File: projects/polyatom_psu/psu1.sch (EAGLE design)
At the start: 2 parts

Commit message: completed psu
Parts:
- added BR1, BR2: (no value), STM_Library:GBU4J
- added C10, C11, C12, C13, C14, C15, C5, C8, C9: 100n, eagle-ltspice:CC1206
- added C100, C2: 1000u, rcl:CPOL-EUE5-13
- added C16, C17, C20, C21: 10u, capacitor-wima:C7.5/3
- added C18: 100n, rcl:C-USC1206
- added C19: 1u, rcl:C-USC1206
- added C3: 0.22u, rcl:C-USC1206
- added C4: 2.2u, rcl:C-USC1206
- added D1, D2: HLMP6, display-hp:HLMP6
- added D3, D4: 1N4004, diode:1N4004
- added R1, R3: 680, eagle-ltspice:R0207/10
- added U$3, U$4, U$5: BANANA, STM_Library:BANANA
- added U$8: TERMINALBLOCK, STM_Library:TERMINALBLOCK
- U$1: value GBU4J -> LM7815; device STM_Library:GBU4J -> STM_Library:LM7815
- U$2: value GBU4J -> LM7915; device STM_Library:GBU4J -> STM_Library:LM7915
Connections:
- new net +15V: C10.1, C11.1, C16.1, C17.1, C18.1, C5.1, C8.1, C9.1, D3.C, R1.2, U$1.P$1, U$3.P$1
- new net -15V: C12.2, C13.2, C14.2, C15.2, C19.2, C20.2, C21.2, D1.K, D4.A, U$2.P$1, U$5.P$1
- new net GND: BR1.P$4, BR2.P$1, C10.2, C100.-, C11.2, C12.1, C13.1, C14.1, C15.1, C16.2, C17.2, C18.2, C19.1, C2.+, C20.1, C21.1, C3.2, C4.1, C5.2, C8.2, C9.2, D2.K, D3.A, D4.C, R3.2, U$1.P$2, U$2.P$2, U$4.P$1, U$8.P$3
- new net N$10: BR2.P$2, U$8.P$2
- new net N$11: BR2.P$3, U$8.P$1
- new net N$2: D2.A, R1.1
- new net N$4: D1.A, R3.1
- new net N$8: BR1.P$2, U$8.P$5
- new net N$9: BR1.P$3, U$8.P$4
- new net NEG: BR2.P$4, C2.-, C4.2, U$2.P$3
- new net POS: BR1.P$1, C100.+, C3.1, U$1.P$3

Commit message: added top and bottom pour, caps renamed
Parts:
- removed C20, C21: 10u, capacitor-wima:C7.5/3
- added C6, C7: 100n, eagle-ltspice:CC1206
- added GND, V2: (no value), wirepad:3,81/1,1
- C11: value 100n -> 1000u; device eagle-ltspice:CC1206 -> rcl:CPOL-EUE5-13
- C12: value 100n -> 2.2u; device eagle-ltspice:CC1206 -> rcl:C-USC1206
- C13: value 100n -> 1u; device eagle-ltspice:CC1206 -> rcl:C-USC1206
- C14, C15, C5: value 100n -> (none); device eagle-ltspice:CC1206 -> rcl:CPOL-USTT2D5
- C16, C17: value 10u -> 100n; device capacitor-wima:C7.5/3 -> eagle-ltspice:CC1206
- C18: device rcl:C-USC1206 -> eagle-ltspice:CC1206
- C19: value 1u -> 100n; device rcl:C-USC1206 -> eagle-ltspice:CC1206
- C2: value 1000u -> 0.22u; device rcl:CPOL-EUE5-13 -> rcl:C-USC1206
- C3: value 0.22u -> 100n
- C4: value 2.2u -> (none); device rcl:C-USC1206 -> rcl:CPOL-USTT2D5
- renumbered C100 to C1, U$2 to U$6
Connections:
- net +15V: now also C3.1, C4.+, C5.+, C6.1, C7.1; no longer C11.1, C16.1, C17.1, C18.1, C5.1
- net -15V: now also C14.-, C15.-, C16.2, C17.2, C18.2, U$6.P$3; no longer C12.2, C14.2, C15.2, C20.2, C21.2, U$6.P$1
- net GND: now also C11.+, C14.+, C15.+, C16.1, C17.1, C18.1, C2.2, C4.-, C5.-, C6.2, C7.2, GND.P, U$6.P$1; no longer C11.2, C14.1, C15.1, C16.2, C17.2, C18.2, C2.+, C20.1, C21.1, C4.1, C5.2, U$6.P$2
- net NEG: now also C11.-, C12.2, U$6.P$2; no longer C2.-, C4.2, U$6.P$3
- net POS: now also C2.1, V2.P; no longer C3.1
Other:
- moved on the sheet: C10, C12, C13, C16, C17, C18, C19, C3, C8, C9

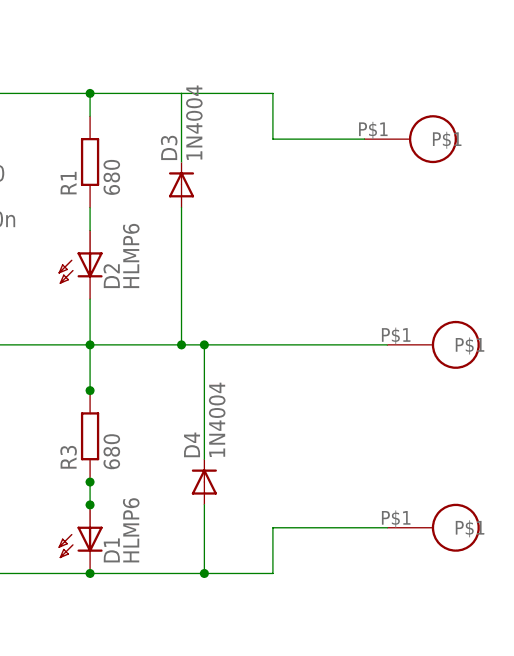
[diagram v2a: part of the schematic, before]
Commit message: added text to the top and bottom of board
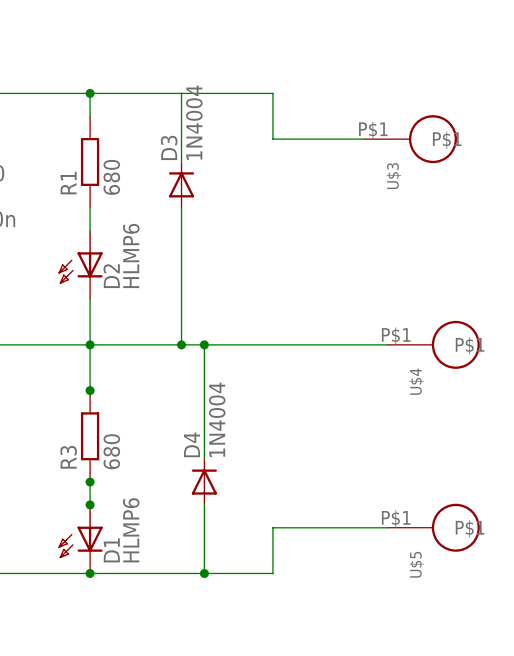
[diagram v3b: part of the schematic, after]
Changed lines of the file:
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@@
 <?xml version="1.0" encoding="utf-8"?>
 <!DOCTYPE eagle SYSTEM "eagle.dtd">
-<eagle version="9.2.2">
+<eagle version="9.2.0">
 <drawing>
 <settings>
@@
 </plain>
 <instances>
-<instance part="C1" gate="G$1" x="55.88" y="66.04" smashed="yes">
+<instance part="C1" gate="G$1" x="55.88" y="66.04">
 <attribute name="NAME" x="57.023" y="66.5226" size="1.778" layer="95"/>
 <attribute name="VALUE" x="57.023" y="61.4426" size="1.778" layer="96"/>
 </instance>
-<instance part="C11" gate="G$1" x="55.88" y="33.02" smashed="yes">
+<instance part="C11" gate="G$1" x="55.88" y="33.02">
 <attribute name="NAME" x="57.023" y="33.5026" size="1.778" layer="95"/>
 <attribute name="VALUE" x="57.023" y="28.4226" size="1.778" layer="96"/>
 </instance>
-<instance part="D1" gate="A" x="170.18" y="25.4" smashed="yes">
+<instance part="D1" gate="A" x="170.18" y="25.4">
 <attribute name="NAME" x="173.482" y="23.876" size="1.778" layer="95" rot="R90"/>
 <attribute name="VALUE" x="175.641" y="23.876" size="1.778" layer="96" rot="R90"/>
 </instance>
-<instance part="D2" gate="A" x="170.18" y="55.88" smashed="yes">
+<instance part="D2" gate="A" x="170.18" y="55.88">
 <attribute name="NAME" x="173.482" y="54.356" size="1.778" layer="95" rot="R90"/>
 <attribute name="VALUE" x="175.641" y="54.356" size="1.778" layer="96" rot="R90"/>
 </instance>
-<instance part="D3" gate="1" x="180.34" y="66.04" smashed="yes" rot="R90">
+<instance part="D3" gate="1" x="180.34" y="66.04" rot="R90">
 <attribute name="NAME" x="179.8574" y="68.58" size="1.778" layer="95" rot="R90"/>
 <attribute name="VALUE" x="182.6514" y="68.58" size="1.778" layer="96" rot="R90"/>
 </instance>
-<instance part="D4" gate="1" x="182.88" y="33.02" smashed="yes" rot="R90">
+<instance part="D4" gate="1" x="182.88" y="33.02" rot="R90">
 <attribute name="NAME" x="182.3974" y="35.56" size="1.778" layer="95" rot="R90"/>
 <attribute name="VALUE" x="185.1914" y="35.56" size="1.778" layer="96" rot="R90"/>
 </instance>
-<instance part="U$3" gate="J$1" x="208.28" y="71.12" smashed="yes" rot="R270"/>
-<instance part="U$4" gate="J$1" x="210.82" y="48.26" smashed="yes" rot="R270"/>
-<instance part="U$5" gate="J$1" x="210.82" y="27.94" smashed="yes" rot="R270"/>
-<instance part="C2" gate="G$1" x="66.04" y="63.5" smashed="yes">
+<instance part="U$3" gate="J$1" x="208.28" y="71.12" rot="R270"/>
+<instance part="U$4" gate="J$1" x="210.82" y="48.26" rot="R270"/>
+<instance part="U$5" gate="J$1" x="210.82" y="27.94" rot="R270"/>
+<instance part="C2" gate="G$1" x="66.04" y="63.5">
 <attribute name="NAME" x="67.056" y="64.135" size="1.778" layer="95"/>
 <attribute name="VALUE" x="67.056" y="59.309" size="1.778" layer="96"/>
 </instance>
-<instance part="C12" gate="G$1" x="66.04" y="33.02" smashed="yes">
+<instance part="C12" gate="G$1" x="66.04" y="33.02">
 <attribute name="NAME" x="67.056" y="33.655" size="1.778" layer="95"/>
 <attribute name="VALUE" x="67.056" y="28.829" size="1.778" layer="96"/>
 </instance>
-<instance part="C3" gate="G$1" x="93.98" y="66.04" smashed="yes">
+<instance part="C3" gate="G$1" x="93.98" y="66.04">
 <attribute name="NAME" x="94.996" y="66.675" size="1.778" layer="95"/>
 <attribute name="VALUE" x="94.996" y="61.849" size="1.778" layer="96"/>
 </instance>
-<instance part="C13" gate="G$1" x="96.52" y="33.02" smashed="yes">
+<instance part="C13" gate="G$1" x="96.52" y="33.02">
 <attribute name="NAME" x="97.536" y="33.655" size="1.778" layer="95"/>
 <attribute name="VALUE" x="97.536" y="28.829" size="1.778" layer="96"/>
 </instance>
-<instance part="C6" gate="G$1" x="124.46" y="66.04" smashed="yes">
+<instance part="C6" gate="G$1" x="124.46" y="66.04">
 <attribute name="NAME" x="125.984" y="66.421" size="1.778" layer="95"/>
 <attribute name="VALUE" x="125.984" y="61.341" size="1.778" layer="96"/>
 </instance>
-<instance part="C7" gate="G$1" x="132.08" y="66.04" smashed="yes">
+<instance part="C7" gate="G$1" x="132.08" y="66.04">
 <attribute name="NAME" x="133.604" y="66.421" size="1.778" layer="95"/>
 <attribute name="VALUE" x="133.604" y="61.341" size="1.778" layer="96"/>
 </instance>
-<instance part="C8" gate="G$1" x="139.7" y="66.04" smashed="yes">
+<instance part="C8" gate="G$1" x="139.7" y="66.04">
 <attribute name="NAME" x="141.224" y="66.421" size="1.778" layer="95"/>
 <attribute name="VALUE" x="141.224" y="61.341" size="1.778" layer="96"/>
 </instance>
-<instance part="C9" gate="G$1" x="147.32" y="66.04" smashed="yes">
+<instance part="C9" gate="G$1" x="147.32" y="66.04">
 <attribute name="NAME" x="148.844" y="66.421" size="1.778" layer="95"/>
 <attribute name="VALUE" x="148.844" y="61.341" size="1.778" layer="96"/>
 </instance>
-<instance part="C10" gate="G$1" x="154.94" y="66.04" smashed="yes">
+<instance part="C10" gate="G$1" x="154.94" y="66.04">
 <attribute name="NAME" x="156.464" y="66.421" size="1.778" layer="95"/>
 <attribute name="VALUE" x="156.464" y="61.341" size="1.778" layer="96"/>
 </instance>
-<instance part="C19" gate="G$1" x="147.32" y="33.02" smashed="yes">
+<instance part="C19" gate="G$1" x="147.32" y="33.02">
 <attribute name="NAME" x="148.844" y="33.401" size="1.778" layer="95"/>
 <attribute name="VALUE" x="148.844" y="28.321" size="1.778" layer="96"/>
 </instance>
-<instance part="C18" gate="G$1" x="139.7" y="33.02" smashed="yes">
+<instance part="C18" gate="G$1" x="139.7" y="33.02">
 <attribute name="NAME" x="141.224" y="33.401" size="1.778" layer="95"/>
 <attribute name="VALUE" x="141.224" y="28.321" size="1.778" layer="96"/>
 </instance>
-<instance part="C17" gate="G$1" x="132.08" y="33.02" smashed="yes">
+<instance part="C17" gate="G$1" x="132.08" y="33.02">
 <attribute name="NAME" x="133.604" y="33.401" size="1.778" layer="95"/>
 <attribute name="VALUE" x="133.604" y="28.321" size="1.778" layer="96"/>
 </instance>
-<instance part="C16" gate="G$1" x="124.46" y="33.02" smashed="yes">
+<instance part="C16" gate="G$1" x="124.46" y="33.02">
 <attribute name="NAME" x="125.984" y="33.401" size="1.778" layer="95"/>
 <attribute name="VALUE" x="125.984" y="28.321" size="1.778" layer="96"/>
 </instance>
-<instance part="U$8" gate="G$1" x="-22.86" y="48.26" smashed="yes" rot="R90"/>
-<instance part="R1" gate="G$1" x="170.18" y="68.58" smashed="yes" rot="R90">
+<instance part="U$8" gate="G$1" x="-22.86" y="48.26" rot="R90"/>
+<instance part="R1" gate="G$1" x="170.18" y="68.58" rot="R90">
 <attribute name="NAME" x="168.6814" y="64.77" size="1.778" layer="95" rot="R90"/>
 <attribute name="VALUE" x="173.482" y="64.77" size="1.778" layer="96" rot="R90"/>
 </instance>
-<instance part="R3" gate="G$1" x="170.18" y="38.1" smashed="yes" rot="R90">
+<instance part="R3" gate="G$1" x="170.18" y="38.1" rot="R90">
 <attribute name="NAME" x="168.6814" y="34.29" size="1.778" layer="95" rot="R90"/>
 <attribute name="VALUE" x="173.482" y="34.29" size="1.778" layer="96" rot="R90"/>
 </instance>
-<instance part="BR1" gate="D1" x="27.94" y="63.5" smashed="yes">
+<instance part="BR1" gate="D1" x="27.94" y="63.5">
 <attribute name="NAME" x="20.32" y="73.66" size="1.27" layer="96"/>
 <attribute name="VALUE" x="20.32" y="53.34" size="1.27" layer="96"/>
 </instance>
-<instance part="BR2" gate="D1" x="27.94" y="33.02" smashed="yes">
+<instance part="BR2" gate="D1" x="27.94" y="33.02">
 <attribute name="NAME" x="20.32" y="43.18" size="1.27" layer="96"/>
 <attribute name="VALUE" x="20.32" y="22.86" size="1.27" layer="96"/>
 </instance>
-<instance part="U$1" gate="G$1" x="78.74" y="76.2" smashed="yes">
+<instance part="U$1" gate="G$1" x="78.74" y="76.2">
 <attribute name="NAME" x="73.66" y="81.28" size="1.27" layer="95"/>
 <attribute name="VALUE" x="78.74" y="81.28" size="1.27" layer="96"/>
 </instance>
-<instance part="SUPPLY1" gate="GND" x="45.72" y="45.72" smashed="yes">
+<instance part="SUPPLY1" gate="GND" x="45.72" y="45.72">
 <attribute name="VALUE" x="43.815" y="42.545" size="1.778" layer="96"/>
 </instance>
-<instance part="U$6" gate="G$1" x="81.28" y="22.86" smashed="yes" rot="MR180">
+<instance part="U$6" gate="G$1" x="81.28" y="22.86" rot="MR180">
 <attribute name="NAME" x="83.82" y="17.78" size="1.27" layer="95" rot="MR180"/>
 <attribute name="VALUE" x="76.2" y="17.78" size="1.27" layer="96" rot="MR180"/>
 </instance>
-<instance part="C4" gate="G$1" x="106.68" y="66.04" smashed="yes">
+<instance part="C4" gate="G$1" x="106.68" y="66.04">
 <attribute name="NAME" x="107.696" y="66.675" size="1.778" layer="95"/>
 <attribute name="VALUE" x="107.696" y="61.849" size="1.778" layer="96"/>
 </instance>
-<instance part="C5" gate="G$1" x="114.3" y="66.04" smashed="yes">
+<instance part="C5" gate="G$1" x="114.3" y="66.04">
 <attribute name="NAME" x="115.316" y="66.675" size="1.778" layer="95"/>
 <attribute name="VALUE" x="115.316" y="61.849" size="1.778" layer="96"/>
 </instance>
-<instance part="C14" gate="G$1" x="106.68" y="33.02" smashed="yes">
+<instance part="C14" gate="G$1" x="106.68" y="33.02">
 <attribute name="NAME" x="107.696" y="33.655" size="1.778" layer="95"/>
 <attribute name="VALUE" x="107.696" y="28.829" size="1.778" layer="96"/>
 </instance>
-<instance part="C15" gate="G$1" x="114.3" y="33.02" smashed="yes">
+<instance part="C15" gate="G$1" x="114.3" y="33.02">
 <attribute name="NAME" x="115.316" y="33.655" size="1.778" layer="95"/>
 <attribute name="VALUE" x="115.316" y="28.829" size="1.778" layer="96"/>
 </instance>
-<instance part="V2" gate="P" x="66.04" y="104.14" smashed="yes" rot="R270">
+<instance part="V2" gate="P" x="66.04" y="104.14" rot="R270">
 <attribute name="NAME" x="67.8942" y="105.283" size="1.778" layer="95" rot="R270"/>
 <attribute name="VALUE" x="62.738" y="105.283" size="1.778" layer="96" rot="R270"/>
 </instance>
-<instance part="GND" gate="P" x="55.88" y="93.98" smashed="yes" rot="R270">
+<instance part="GND" gate="P" x="55.88" y="93.98" rot="R270">
 <attribute name="NAME" x="57.7342" y="95.123" size="1.778" layer="95" rot="R270"/>
 <attribute name="VALUE" x="52.578" y="95.123" size="1.778" layer="96" rot="R270"/>
